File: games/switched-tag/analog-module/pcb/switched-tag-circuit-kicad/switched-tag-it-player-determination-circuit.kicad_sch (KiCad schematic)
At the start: 16 parts

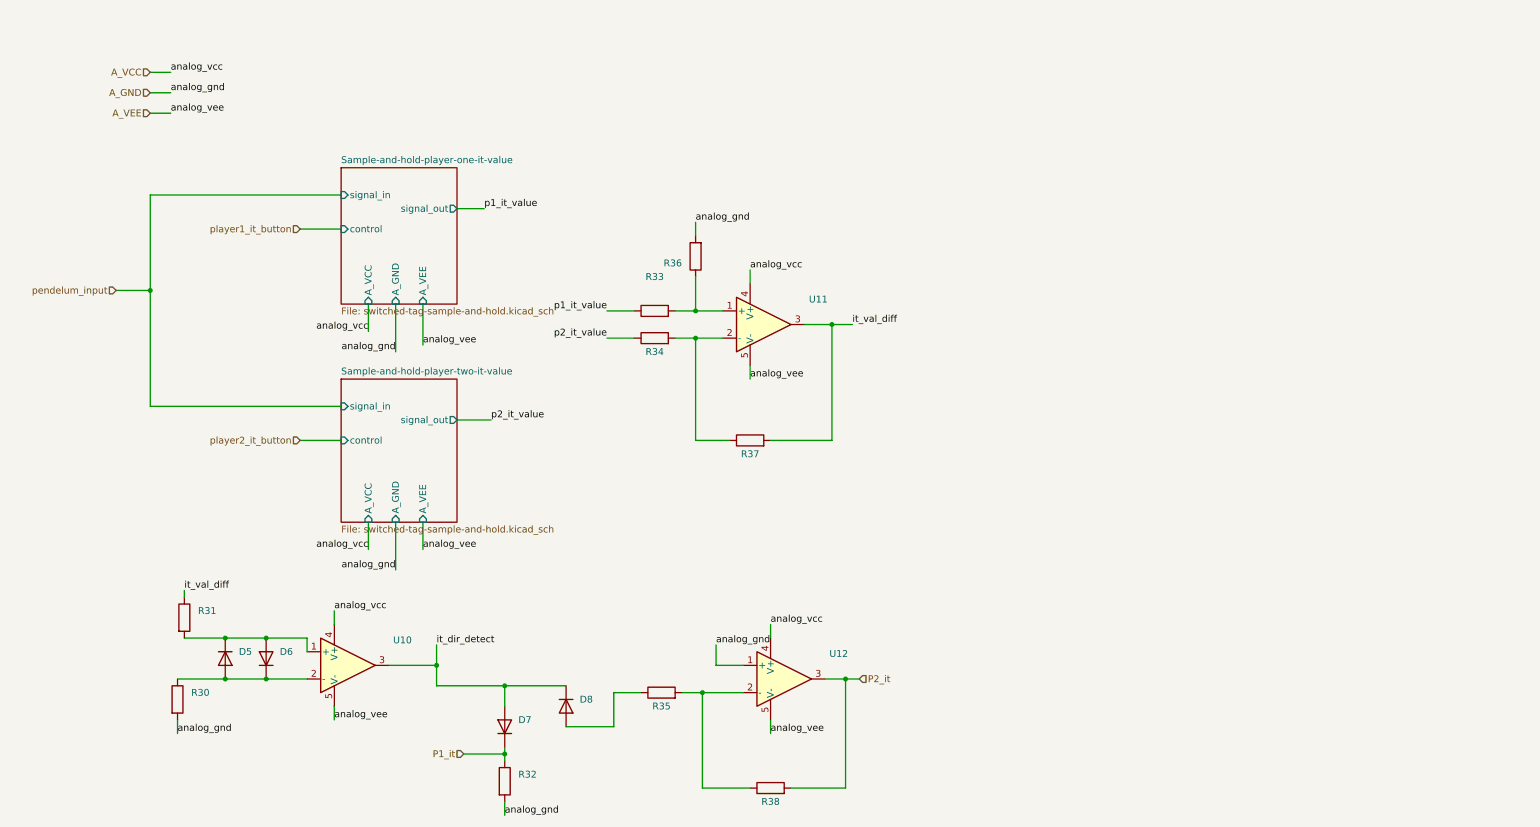
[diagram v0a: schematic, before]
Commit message: Converted Lm358.mod to .lib file for convenience.
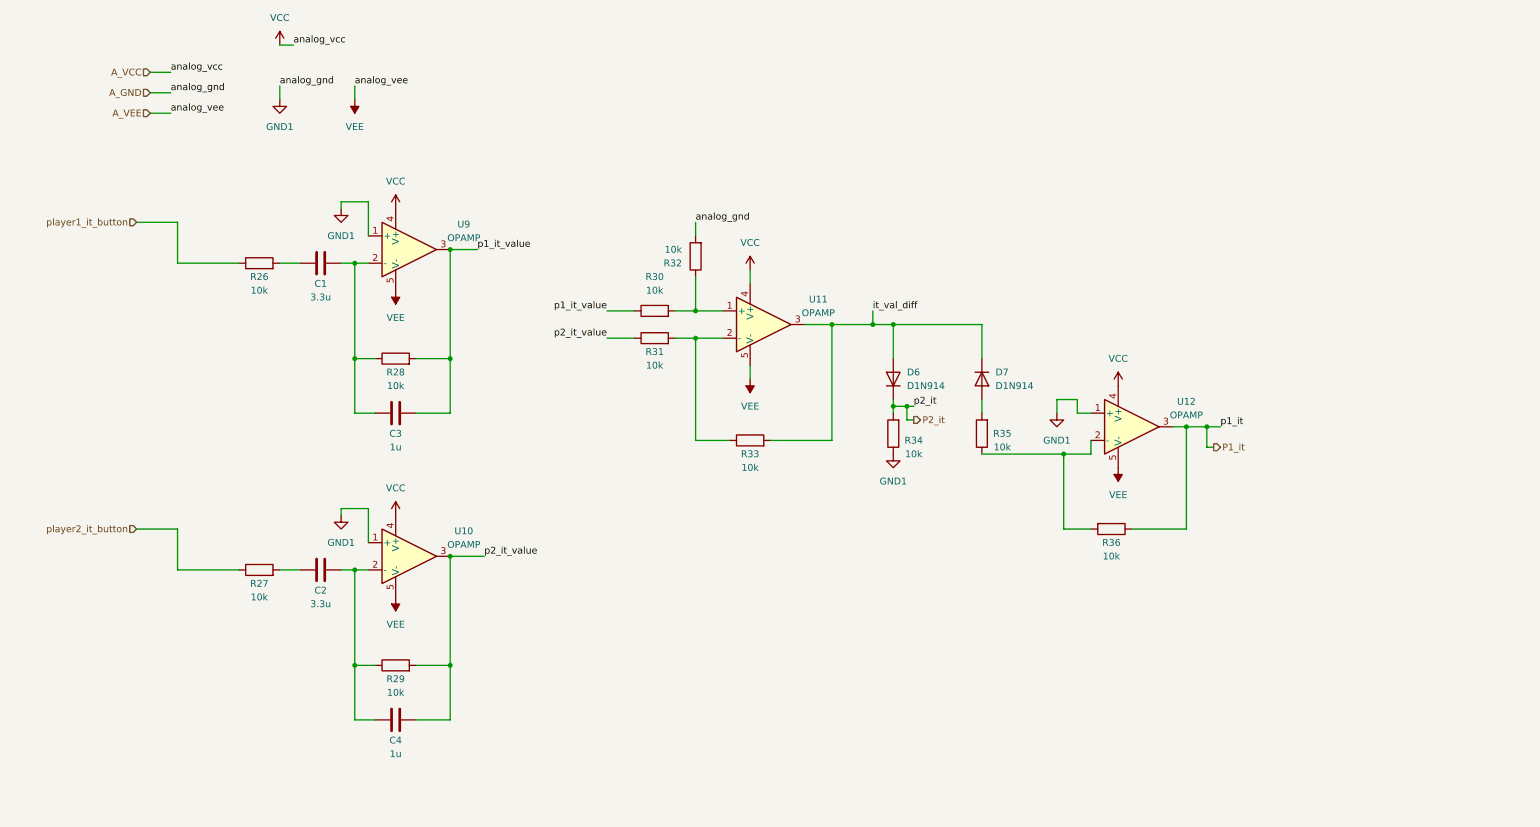
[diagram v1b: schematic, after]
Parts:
- removed D7, D8: (no value), symbol Device:D
- removed R30, R31, R32, R38: (no value), symbol Device:R
- removed U12: (no value), symbol Simulation_SPICE:OPAMP
- added C1, C2: 3.3u, symbol Device:C
- added C3, C4: 1u, symbol Device:C
- added R26, R27, R28, R29, R34, R36: 10k, symbol Device:R
- added U10, U9: OPAMP, symbol Simulation_SPICE:OPAMP
- D6: renamed from D5; value (none) -> D1N914; Spice_Lib_File ../../../../../spice-models/1N914.lib -> (none); Spice_Model D1N914 -> (none); Spice_Netlist_Enabled Y -> (none); Spice_Node_Sequence 2 1 -> (none); Spice_Primitive D -> (none)
- D7: renamed from D6; value (none) -> D1N914; Spice_Lib_File ../../../../../spice-models/1N914.lib -> (none); Spice_Model D1N914 -> (none); Spice_Netlist_Enabled Y -> (none); Spice_Node_Sequence 2 1 -> (none); Spice_Primitive D -> (none)
- R30: renamed from R33; value (none) -> 10k
- R31: renamed from R34; value (none) -> 10k
- R32: renamed from R36; value (none) -> 10k
- R33: renamed from R37; value (none) -> 10k
- R35: value (none) -> 10k
- U11: value (none) -> OPAMP; Spice_Lib_File /home/pab/Inventions/analog-circuit-game-console/ms-circuit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 -> (none); Spice_Model AD8031 -> (none); Spice_Netlist_Enabled Y -> (none); Spice_Node_Sequence 1 2 4 5 3 -> (none); Spice_Primitive X -> (none)
- U12: renamed from U10; value (none) -> OPAMP; Spice_Lib_File /home/pab/Inventions/analog-circuit-game-console/ms-circuit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 -> (none); Spice_Model AD8031 -> (none); Spice_Netlist_Enabled Y -> (none); Spice_Node_Sequence 1 2 4 5 3 -> (none); Spice_Primitive X -> (none)
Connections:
- net it_dir_detect is gone; now on net P1_it: U12.3
- net P1_it: now also R36.1
- net P2_it: now also D6.1 (K), R34.2
- net it_val_diff: now also D6.2 (A), D7.1 (K)
- net p1_it_value: now also C3.1, R28.2, U9.3
- net p2_it_value: now also C4.1, R29.2, U10.3
- net player1_it_button: now also R26.1
- net player2_it_button: now also R27.1
- net at R35.1: now also U12.2 (-), R36.2
- net at R35.2: now also D7.2 (A)
- net A_GND renamed GND1
- net GND1: now also U12.1 (+), R34.1, U10.1 (+), U9.1 (+)
- net A_VCC renamed VCC
- net VCC: now also U10.4 (V+), U9.4 (V+)
- net A_VEE renamed VEE
- net VEE: now also U10.5 (V-), U9.5 (V-)
- new net: C2.1, C4.2, R29.1, U10.2 (-)
- new net: C1.1, C3.2, R28.1, U9.2 (-)
- new net: C2.2, R27.2
- new net: C1.2, R26.2
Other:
- removed sheet Sample-and-hold-player-one-it-value
- removed sheet Sample-and-hold-player-two-it-value
- moved on the sheet: D6, D7, U12

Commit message: Updated simulation schematic. Need to fix timestep too small problem.
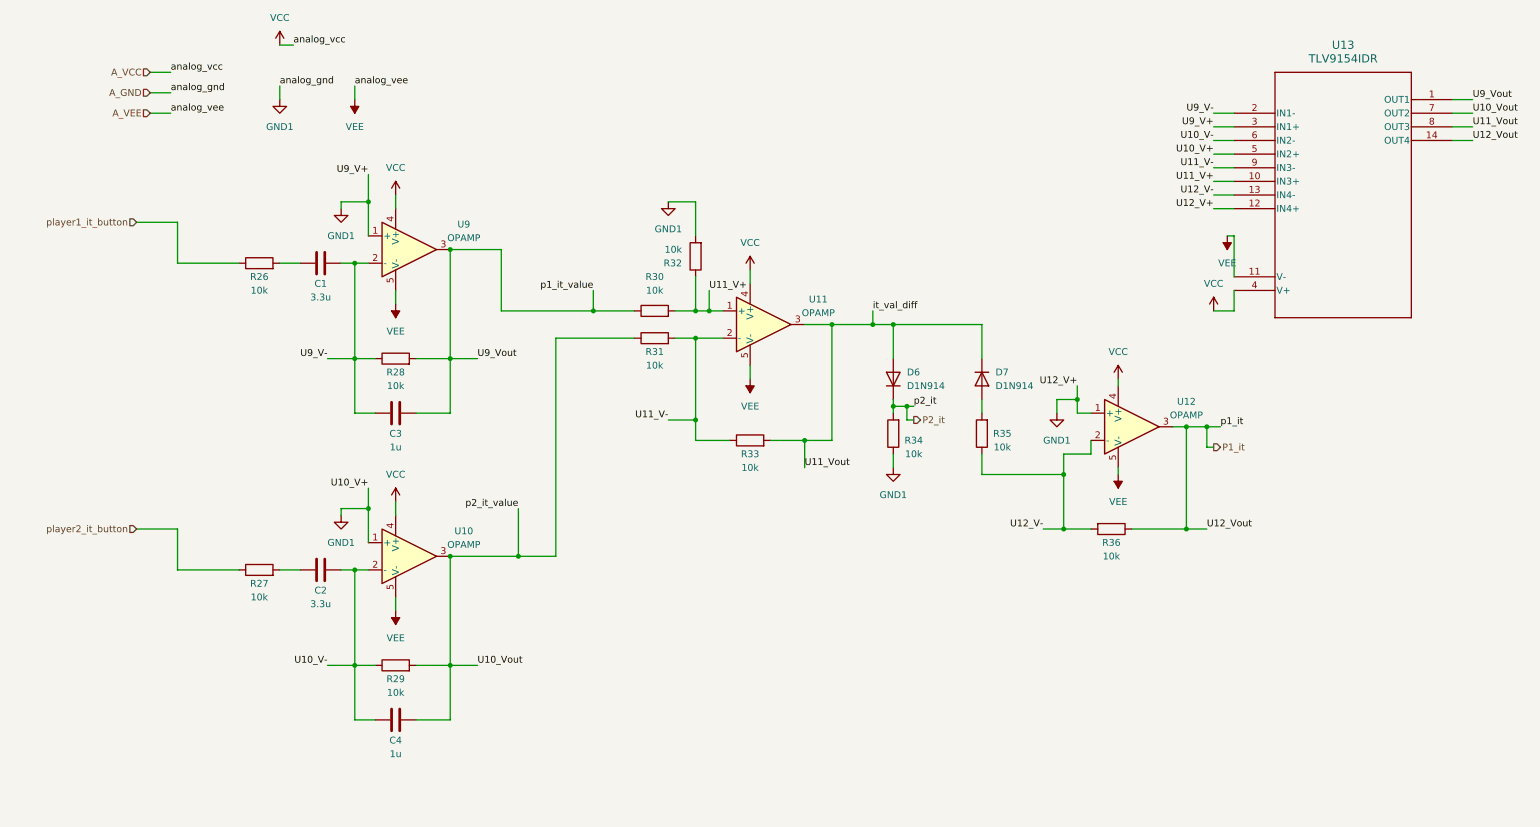
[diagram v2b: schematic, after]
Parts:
- added U13: TLV9154IDR, SOIC_9154IDR_TEX, symbol switched-tag-symbol-lib:TLV9154IDR
- U10, U11, U12, U9: now left out of the parts list
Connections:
- net GND1: now also U13.12 (IN4+), U13.3 (IN1+), U13.5 (IN2+)
- net P1_it: now also U13.14 (OUT4)
- net VCC: now also U13.4 (V+)
- net VEE: now also U13.11 (V-)
- net U10_V-: now reaches C2.1, C4.2, R29.1, U10.2 (-)
- net U10_V-: now also U13.6 (IN2-)
- net U12_V-: now reaches R35.1, R36.2, U12.2 (-)
- net U12_V-: now also U13.13 (IN4-)
- net U9_V-: now reaches C1.1, C3.2, R28.1, U9.2 (-)
- net U9_V-: now also U13.2 (IN1-)
- net U11_V+: now reaches R30.2, R32.1, U11.1 (+)
- net U11_V+: now also U13.10 (IN3+)
- net U11_V-: now reaches R31.2, R33.1, U11.2 (-)
- net U11_V-: now also U13.9 (IN3-)
- net it_val_diff renamed U11_Vout
- net U11_Vout: now also U13.8 (OUT3)
- net p1_it_value renamed U9_Vout
- net U9_Vout: now also U13.1 (OUT1)
- net p2_it_value renamed U10_Vout
- net U10_Vout: now also U13.7 (OUT2)

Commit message: Started pcb with placeholder components. Incomplete PCB.
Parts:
- C1, C2, C3, C4: footprint (none) -> Capacitor_SMD:C_0603_1608Metric
- D6, D7: footprint (none) -> Diode_SMD:D_0603_1608Metric
- R26, R27, R28, R29, R30, R31, R32, R33, R34, R35, R36: footprint (none) -> Resistor_SMD:R_0603_1608Metric
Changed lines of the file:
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@@
       (effects (font (size 1.27 1.27)))
     )
-    (property "Footprint" "" (at 80.01 155.9052 0)
+    (property "Footprint" "Capacitor_SMD:C_0603_1608Metric" (at 80.01 155.9052 0)
       (effects (font (size 1.27 1.27)) hide)
     )
@@
       (effects (font (size 1.27 1.27)))
     )
-    (property "Footprint" "" (at 178.308 101.6 90)
+    (property "Footprint" "Resistor_SMD:R_0603_1608Metric" (at 178.308 101.6 90)
       (effects (font (size 1.27 1.27)) hide)
     )
@@
       (effects (font (size 1.27 1.27)))
     )
-    (property "Footprint" "" (at 83.82 146.558 90)
+    (property "Footprint" "Resistor_SMD:R_0603_1608Metric" (at 83.82 146.558 90)
       (effects (font (size 1.27 1.27)) hide)
     )
@@
       (effects (font (size 1.27 1.27)))
     )
-    (property "Footprint" "" (at 58.42 128.778 90)
+    (property "Footprint" "Resistor_SMD:R_0603_1608Metric" (at 58.42 128.778 90)
       (effects (font (size 1.27 1.27)) hide)
     )
@@
       (effects (font (size 1.27 1.27)))
     )
-    (property "Footprint" "" (at 83.82 89.408 90)
+    (property "Footprint" "Resistor_SMD:R_0603_1608Metric" (at 83.82 89.408 90)
       (effects (font (size 1.27 1.27)) hide)
     )
@@
       (effects (font (size 1.27 1.27)))
     )
-    (property "Footprint" "" (at 132.08 80.518 90)
+    (property "Footprint" "Resistor_SMD:R_0603_1608Metric" (at 132.08 80.518 90)
       (effects (font (size 1.27 1.27)) hide)
     )
@@
       (effects (font (size 1.27 1.27)))
     )
-    (property "Footprint" "" (at 194.818 101.6 90)
+    (property "Footprint" "Resistor_SMD:R_0603_1608Metric" (at 194.818 101.6 90)
       (effects (font (size 1.27 1.27)) hide)
     )
@@
       (effects (font (size 1.27 1.27)))
     )
-    (property "Footprint" "" (at 80.01 98.7552 0)
+    (property "Footprint" "Capacitor_SMD:C_0603_1608Metric" (at 80.01 98.7552 0)
       (effects (font (size 1.27 1.27)) hide)
     )
@@
       (effects (font (size 1.27 1.27)) (justify right))
     )
-    (property "Footprint" "" (at 176.53 91.44 0)
+    (property "Footprint" "Diode_SMD:D_0603_1608Metric" (at 176.53 91.44 0)
       (effects (font (size 1.27 1.27)) hide)
     )
@@
       (effects (font (size 1.27 1.27)))
     )
-    (property "Footprint" "" (at 66.04 127.9652 0)
+    (property "Footprint" "Capacitor_SMD:C_0603_1608Metric" (at 66.04 127.9652 0)
       (effects (font (size 1.27 1.27)) hide)
     )
@@
       (effects (font (size 1.27 1.27)))
     )
-    (property "Footprint" "" (at 66.04 70.8152 0)
+    (property "Footprint" "Capacitor_SMD:C_0603_1608Metric" (at 66.04 70.8152 0)
       (effects (font (size 1.27 1.27)) hide)
     )
@@
       (effects (font (size 1.27 1.27)))
     )
-    (property "Footprint" "" (at 149.86 104.648 90)
+    (property "Footprint" "Resistor_SMD:R_0603_1608Metric" (at 149.86 104.648 90)
       (effects (font (size 1.27 1.27)) hide)
     )
@@
       (effects (font (size 1.27 1.27)))
     )
-    (property "Footprint" "" (at 132.08 85.598 90)
+    (property "Footprint" "Resistor_SMD:R_0603_1608Metric" (at 132.08 85.598 90)
       (effects (font (size 1.27 1.27)) hide)
     )
@@
       (effects (font (size 1.27 1.27)) (justify left))
     )
-    (property "Footprint" "" (at 193.04 91.44 0)
+    (property "Footprint" "Diode_SMD:D_0603_1608Metric" (at 193.04 91.44 0)
       (effects (font (size 1.27 1.27)) hide)
     )
@@
       (effects (font (size 1.27 1.27)))
     )
-    (property "Footprint" "" (at 58.42 71.628 90)
+    (property "Footprint" "Resistor_SMD:R_0603_1608Metric" (at 58.42 71.628 90)
       (effects (font (size 1.27 1.27)) hide)
     )
@@
       (effects (font (size 1.27 1.27)) (justify left))
     )
-    (property "Footprint" "" (at 141.478 68.58 90)
+    (property "Footprint" "Resistor_SMD:R_0603_1608Metric" (at 141.478 68.58 90)
       (effects (font (size 1.27 1.27)) hide)
     )
@@
       (effects (font (size 1.27 1.27)))
     )
-    (property "Footprint" "" (at 217.17 117.602 90)
-      (effects (font (size 1.27 1.27)) hide)
-    )
+    (property "Footprint" "Resistor_SMD:R_0603_1608Metric" (at 217.17 117.602 90)
+      (effects (font (size 1.27 1.27)) hide)
+    )

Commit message: Saving pcb placement.
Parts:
- U13: footprint SOIC_9154IDR_TEX -> switched-tag-footprint-lib:SOIC_9154IDR_TEX
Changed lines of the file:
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@@
       (effects (font (size 1.524 1.524)))
     )
-    (property "Footprint" "SOIC_9154IDR_TEX" (at 240.03 41.91 0)
+    (property "Footprint" "switched-tag-footprint-lib:SOIC_9154IDR_TEX" (at 240.03 41.91 0)
       (effects (font (size 1.27 1.27) italic) hide)
     )

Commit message: Changed component size from 0603 to 0805 for easier hand soldering.
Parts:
- C1, C2, C3, C4: footprint Capacitor_SMD:C_0603_1608Metric -> Capacitor_SMD:C_0805_2012Metric
- D6, D7: footprint Diode_SMD:D_0603_1608Metric -> Diode_SMD:D_0805_2012Metric
- R26, R27, R28, R29, R30, R31, R32, R33, R34, R35, R36: footprint Resistor_SMD:R_0603_1608Metric -> Resistor_SMD:R_0805_2012Metric
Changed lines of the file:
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@@
       (effects (font (size 1.27 1.27)))
     )
-    (property "Footprint" "Capacitor_SMD:C_0603_1608Metric" (at 80.01 155.9052 0)
+    (property "Footprint" "Capacitor_SMD:C_0805_2012Metric" (at 80.01 155.9052 0)
       (effects (font (size 1.27 1.27)) hide)
     )
@@
       (effects (font (size 1.27 1.27)))
     )
-    (property "Footprint" "Resistor_SMD:R_0603_1608Metric" (at 178.308 101.6 90)
+    (property "Footprint" "Resistor_SMD:R_0805_2012Metric" (at 178.308 101.6 90)
       (effects (font (size 1.27 1.27)) hide)
     )
@@
       (effects (font (size 1.27 1.27)))
     )
-    (property "Footprint" "Resistor_SMD:R_0603_1608Metric" (at 83.82 146.558 90)
+    (property "Footprint" "Resistor_SMD:R_0805_2012Metric" (at 83.82 146.558 90)
       (effects (font (size 1.27 1.27)) hide)
     )
@@
       (effects (font (size 1.27 1.27)))
     )
-    (property "Footprint" "Resistor_SMD:R_0603_1608Metric" (at 58.42 128.778 90)
+    (property "Footprint" "Resistor_SMD:R_0805_2012Metric" (at 58.42 128.778 90)
       (effects (font (size 1.27 1.27)) hide)
     )
@@
       (effects (font (size 1.27 1.27)))
     )
-    (property "Footprint" "Resistor_SMD:R_0603_1608Metric" (at 83.82 89.408 90)
+    (property "Footprint" "Resistor_SMD:R_0805_2012Metric" (at 83.82 89.408 90)
       (effects (font (size 1.27 1.27)) hide)
     )
@@
       (effects (font (size 1.27 1.27)))
     )
-    (property "Footprint" "Resistor_SMD:R_0603_1608Metric" (at 132.08 80.518 90)
+    (property "Footprint" "Resistor_SMD:R_0805_2012Metric" (at 132.08 80.518 90)
       (effects (font (size 1.27 1.27)) hide)
     )
@@
       (effects (font (size 1.27 1.27)))
     )
-    (property "Footprint" "Resistor_SMD:R_0603_1608Metric" (at 194.818 101.6 90)
+    (property "Footprint" "Resistor_SMD:R_0805_2012Metric" (at 194.818 101.6 90)
       (effects (font (size 1.27 1.27)) hide)
     )
@@
       (effects (font (size 1.27 1.27)))
     )
-    (property "Footprint" "Capacitor_SMD:C_0603_1608Metric" (at 80.01 98.7552 0)
+    (property "Footprint" "Capacitor_SMD:C_0805_2012Metric" (at 80.01 98.7552 0)
       (effects (font (size 1.27 1.27)) hide)
     )
@@
       (effects (font (size 1.27 1.27)) (justify right))
     )
-    (property "Footprint" "Diode_SMD:D_0603_1608Metric" (at 176.53 91.44 0)
+    (property "Footprint" "Diode_SMD:D_0805_2012Metric" (at 176.53 91.44 0)
       (effects (font (size 1.27 1.27)) hide)
     )
@@
       (effects (font (size 1.27 1.27)))
     )
-    (property "Footprint" "Capacitor_SMD:C_0603_1608Metric" (at 66.04 127.9652 0)
+    (property "Footprint" "Capacitor_SMD:C_0805_2012Metric" (at 66.04 127.9652 0)
       (effects (font (size 1.27 1.27)) hide)
     )
@@
       (effects (font (size 1.27 1.27)))
     )
-    (property "Footprint" "Capacitor_SMD:C_0603_1608Metric" (at 66.04 70.8152 0)
+    (property "Footprint" "Capacitor_SMD:C_0805_2012Metric" (at 66.04 70.8152 0)
       (effects (font (size 1.27 1.27)) hide)
     )
@@
       (effects (font (size 1.27 1.27)))
     )
-    (property "Footprint" "Resistor_SMD:R_0603_1608Metric" (at 149.86 104.648 90)
+    (property "Footprint" "Resistor_SMD:R_0805_2012Metric" (at 149.86 104.648 90)
       (effects (font (size 1.27 1.27)) hide)
     )
@@
       (effects (font (size 1.27 1.27)))
     )
-    (property "Footprint" "Resistor_SMD:R_0603_1608Metric" (at 132.08 85.598 90)
+    (property "Footprint" "Resistor_SMD:R_0805_2012Metric" (at 132.08 85.598 90)
       (effects (font (size 1.27 1.27)) hide)
     )
@@
       (effects (font (size 1.27 1.27)) (justify left))
     )
-    (property "Footprint" "Diode_SMD:D_0603_1608Metric" (at 193.04 91.44 0)
+    (property "Footprint" "Diode_SMD:D_0805_2012Metric" (at 193.04 91.44 0)
       (effects (font (size 1.27 1.27)) hide)
     )
@@
       (effects (font (size 1.27 1.27)))
     )
-    (property "Footprint" "Resistor_SMD:R_0603_1608Metric" (at 58.42 71.628 90)
+    (property "Footprint" "Resistor_SMD:R_0805_2012Metric" (at 58.42 71.628 90)
       (effects (font (size 1.27 1.27)) hide)
     )
@@
       (effects (font (size 1.27 1.27)) (justify left))
     )
-    (property "Footprint" "Resistor_SMD:R_0603_1608Metric" (at 141.478 68.58 90)
+    (property "Footprint" "Resistor_SMD:R_0805_2012Metric" (at 141.478 68.58 90)
       (effects (font (size 1.27 1.27)) hide)
     )
@@
       (effects (font (size 1.27 1.27)))
     )
-    (property "Footprint" "Resistor_SMD:R_0603_1608Metric" (at 217.17 117.602 90)
-      (effects (font (size 1.27 1.27)) hide)
-    )
+    (property "Footprint" "Resistor_SMD:R_0805_2012Metric" (at 217.17 117.602 90)
+      (effects (font (size 1.27 1.27)) hide)
+    )
